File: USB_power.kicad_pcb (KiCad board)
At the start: 2 copper layers, 42.5 x 65.5 mm, 30 parts, among them J1 PWR_IN, J2 USB_A_Stacked, J3 Power_check, J4 USB_C_Receptacle_USB2.0_16P, J5 USB_A

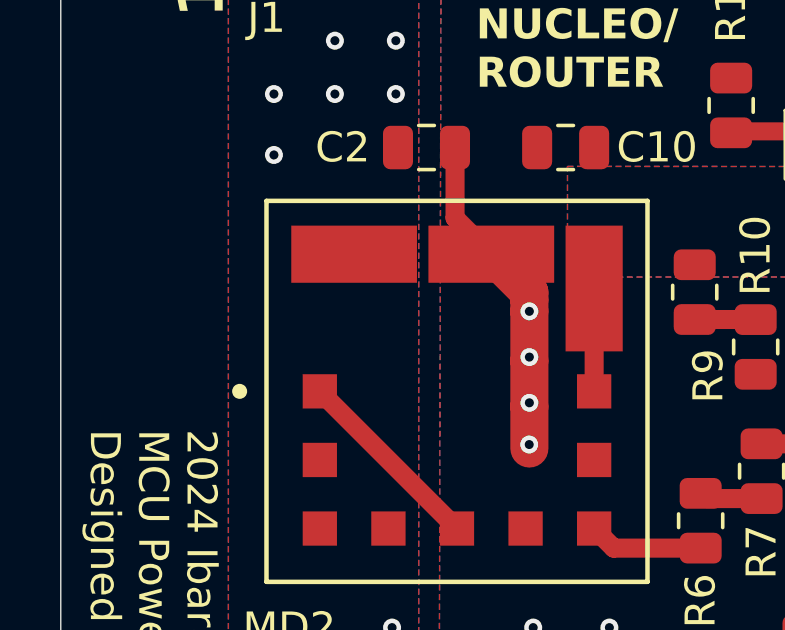
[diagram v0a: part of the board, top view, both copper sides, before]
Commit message: MD2直下BATTビア調整
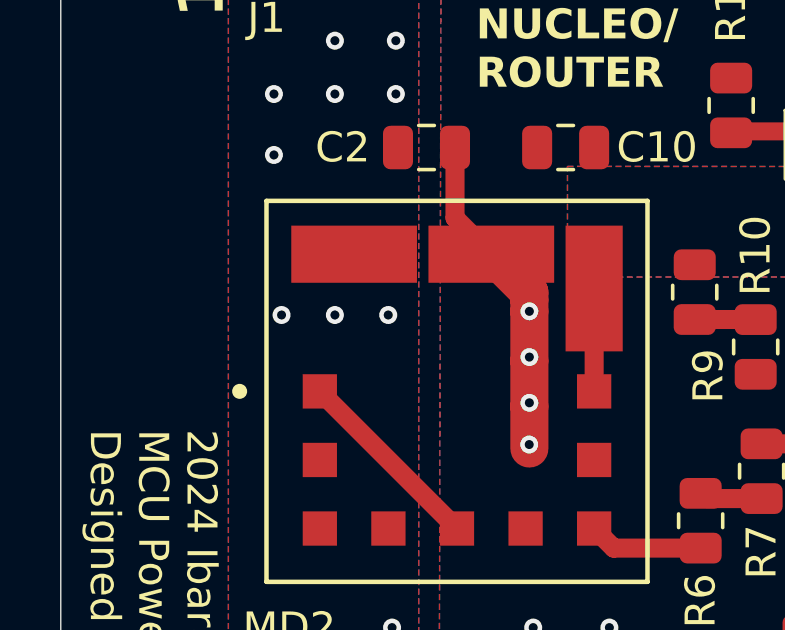
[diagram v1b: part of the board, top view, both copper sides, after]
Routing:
- net +BATT: vias 12 -> 15
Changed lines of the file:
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@@
+	)
+	(via
+		(at 136.906 98.552)
+		(size 0.6)
+		(drill 0.3)
+		(layers "F.Cu" "B.Cu")
+		(free yes)
+		(net 11)
+	)
+	(via
+		(at 135.128 98.552)
+		(size 0.6)
+		(drill 0.3)
+		(layers "F.Cu" "B.Cu")
+		(free yes)
+		(net 11)
 	)
 	(via
@@
 		(size 0.6)
 		(drill 0.3)
+		(layers "F.Cu" "B.Cu")
+		(free yes)
+		(net 11)
+	)
+	(via
+		(at 138.684 98.552)
+		(size 0.6)
+		(drill 0.3)

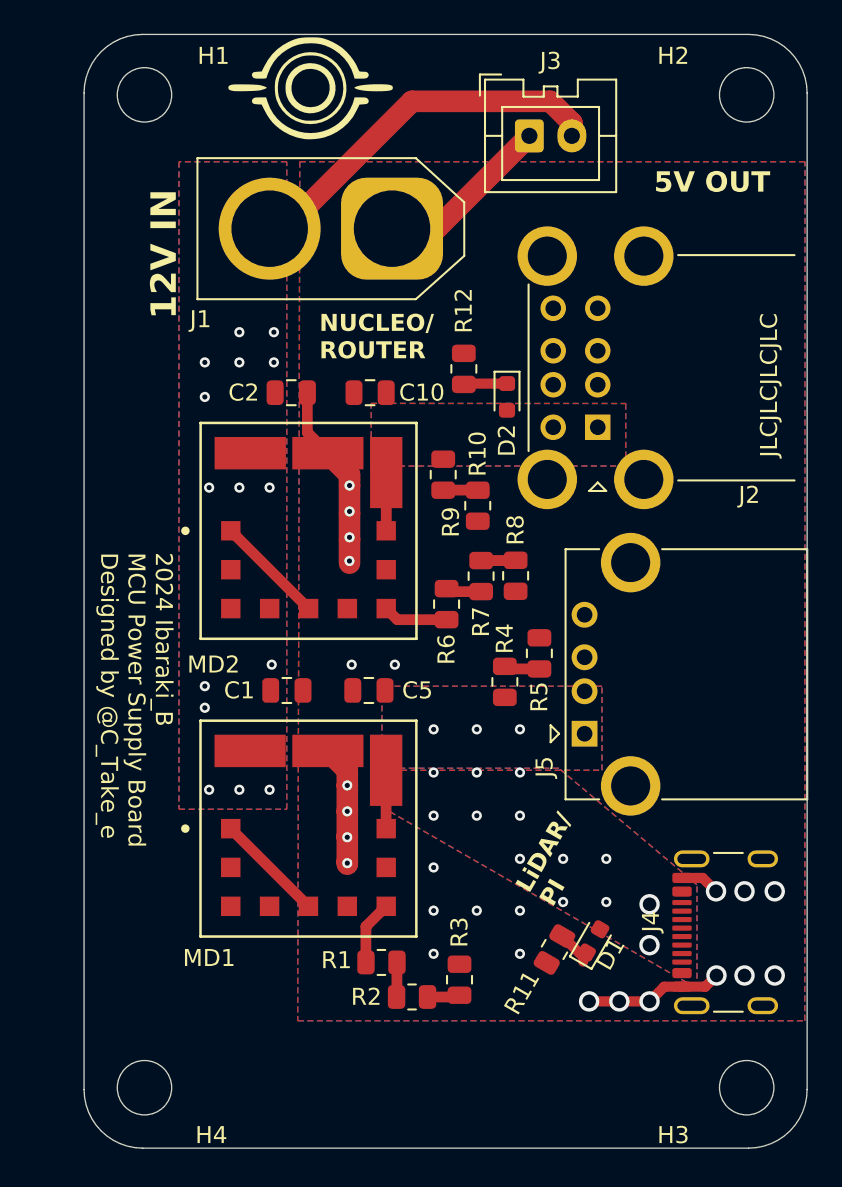
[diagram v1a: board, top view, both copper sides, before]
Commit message: Cのスペース詰めてGNDベタ回り込み
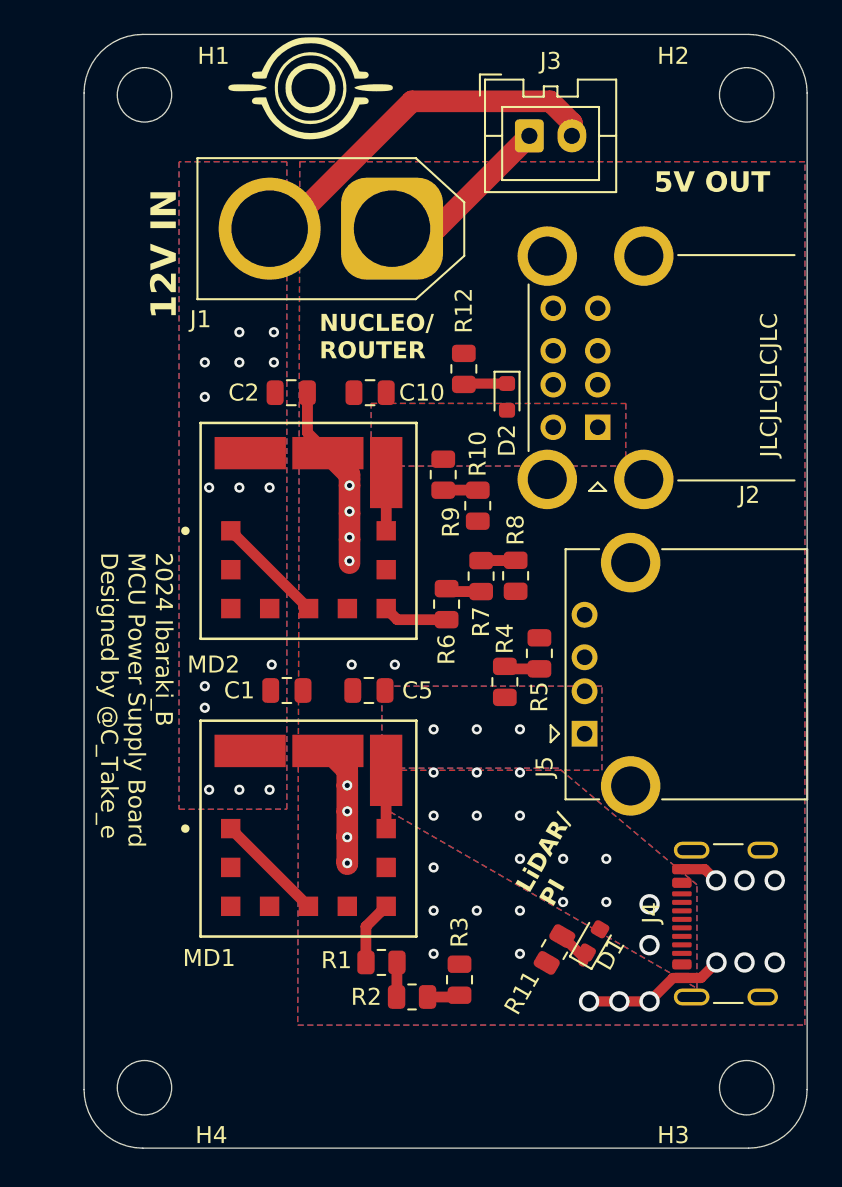
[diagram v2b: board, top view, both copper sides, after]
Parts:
- moved J4 0.51 mm to (166.6, 124.2)
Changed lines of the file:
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@@
 	(footprint "Connector_USB:USB_C_Receptacle_GCT_USB4105-xx-A_16P_TopMnt_Horizontal"
 		(layer "F.Cu")
-		(at 166.629518 124.719518 90)
+		(at 166.624 124.206 90)
 		(descr "USB 2.0 Type C Receptacle, GCT, 16P, top mounted, horizontal, 5A: https://gct.co/files/drawings/usb4105.pdf")
 		(tags "USB C Type-C Receptacle SMD USB 2.0 16P 16C USB4105-15-A USB4105-15-A-060 USB4105-15-A-120 USB4105-GF-A USB4105-GF-A-060 USB4105-GF-A-120")
@@
 	)
 	(segment
-		(start 164.318518 127.919518)
-		(end 162.949518 127.919518)
-		(width 0.6)
-		(layer "F.Cu")
-		(net 1)
-	)
-	(segment
 		(start 153.167518 104.653518)
 		(end 152.937018 104.653518)
@@
 	)
 	(segment
-		(start 164.166118 121.519518)
-		(end 162.949518 121.519518)
+		(start 162.944 121.006)
+		(end 164.293118 121.006)
 		(width 0.6)
 		(layer "F.Cu")
@@
 	)
 	(segment
-		(start 164.953118 122.306518)
-		(end 164.851118 122.408518)
+		(start 162.944 127.406)
+		(end 162.419036 127.406)
 		(width 0.6)
 		(layer "F.Cu")
@@
 	)
 	(segment
-		(start 162.949518 127.919518)
-		(end 161.905518 127.919518)
-		(width 0.6)
-		(layer "F.Cu")
-		(net 1)
-	)
-	(segment
 		(start 143.256 120.523)
 		(end 143.256 119.126)
@@
 	)
 	(segment
-		(start 164.978518 127.259518)
-		(end 164.318518 127.919518)
-		(width 0.6)
-		(layer "F.Cu")
-		(net 1)
-	)
-	(segment
 		(start 140.97 123.19)
 		(end 140.97 122.9995)
@@
 	)
 	(segment
-		(start 164.953118 122.306518)
-		(end 164.166118 121.519518)
+		(start 162.419036 127.406)
+		(end 161.041518 128.783518)
 		(width 0.6)
 		(layer "F.Cu")
@@
 	)
 	(segment
+		(start 162.944 127.406)
+		(end 164.064518 127.406)
+		(width 0.6)
+		(layer "F.Cu")
+		(net 1)
+	)
+	(segment
 		(start 143.388518 97.795518)
 		(end 143.388518 98.049518)
@@
 	)
 	(segment
+		(start 164.064518 127.406)
+		(end 164.978518 126.492)
+		(width 0.6)
+		(layer "F.Cu")
+		(net 1)
+	)
+	(segment
 		(start 157.485518 128.783518)
 		(end 161.041518 128.783518)
@@
 	)
 	(segment
+		(start 164.293118 121.006)
+		(end 164.953118 121.666)
+		(width 0.6)
+		(layer "F.Cu")
+		(net 1)
+	)
+	(segment
 		(start 143.256 117.602)
 		(end 143.256 116.078)
@@
 		(net 1)
 	)
-	(segment
-		(start 161.905518 127.919518)
-		(end 161.041518 128.783518)
-		(width 0.6)
-		(layer "F.Cu")
-		(net 1)
-	)
 	(via
 		(at 143.383 102.87)
@@
 	)
 	(via
-		(at 166.629518 122.306518)
+		(at 166.629518 121.666)
 		(size 1.2)
 		(drill 0.8)
@@
 	)
 	(via
-		(at 164.978518 127.259518)
+		(at 164.978518 126.492)
 		(size 1.2)
 		(drill 0.8)
@@
 	)
 	(via
-		(at 164.953118 122.306518)
+		(at 164.953118 121.666)
 		(size 1.2)
 		(drill 0.8)
@@
 	)
 	(via
-		(at 166.629518 127.259518)
+		(at 166.629518 126.492)
 		(size 1.2)
 		(drill 0.8)
@@
 	)
 	(via
-		(at 168.407518 127.259518)
+		(at 168.407518 126.492)
 		(size 1.2)
 		(drill 0.8)
@@
 	)
 	(via
-		(at 168.407518 122.306518)
+		(at 168.407518 121.666)
 		(size 1.2)
 		(drill 0.8)
@@
 		(polygon
 			(pts
-				(xy 140.462 79.375) (xy 140.340518 129.926518) (xy 170.18 129.921) (xy 170.185518 79.375)
+				(xy 140.462 79.375) (xy 140.340518 130.180518) (xy 170.18 130.175) (xy 170.185518 79.375)
 			)
 		)

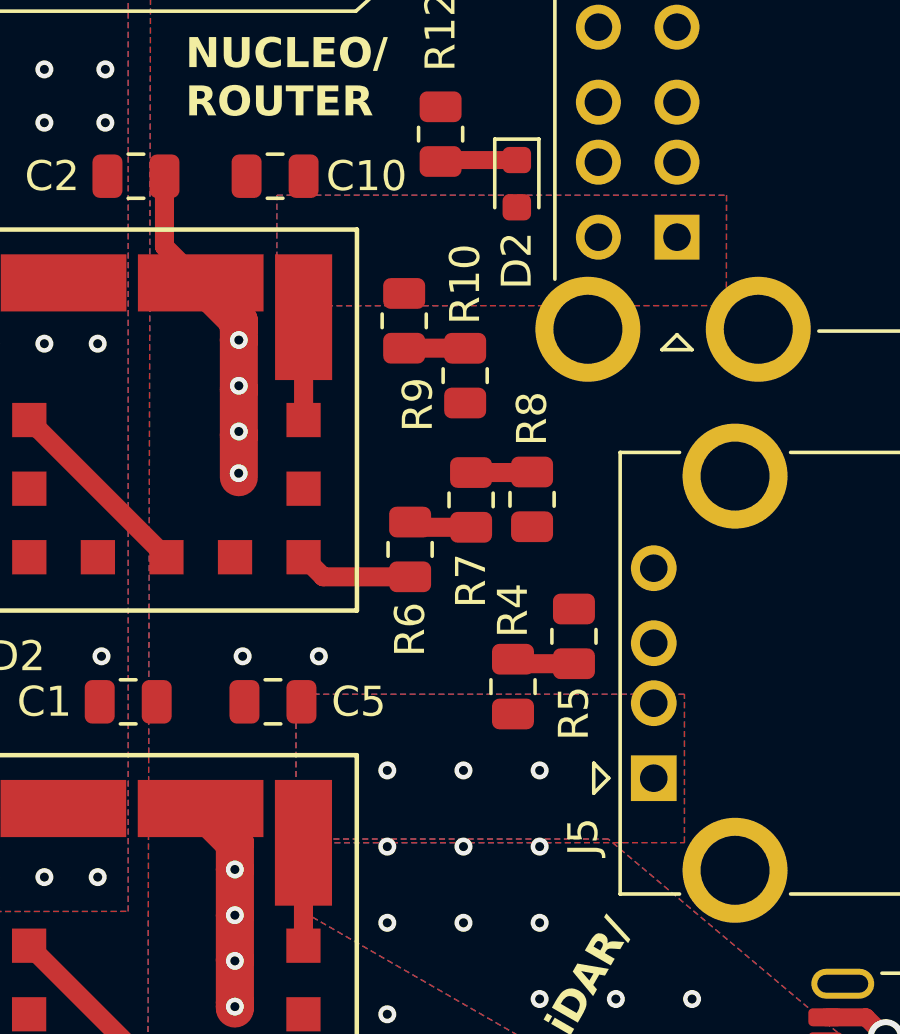
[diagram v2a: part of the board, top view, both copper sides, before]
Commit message: MD2周り抵抗ゴン詰め、MD1系統スタックコネクタ化計画
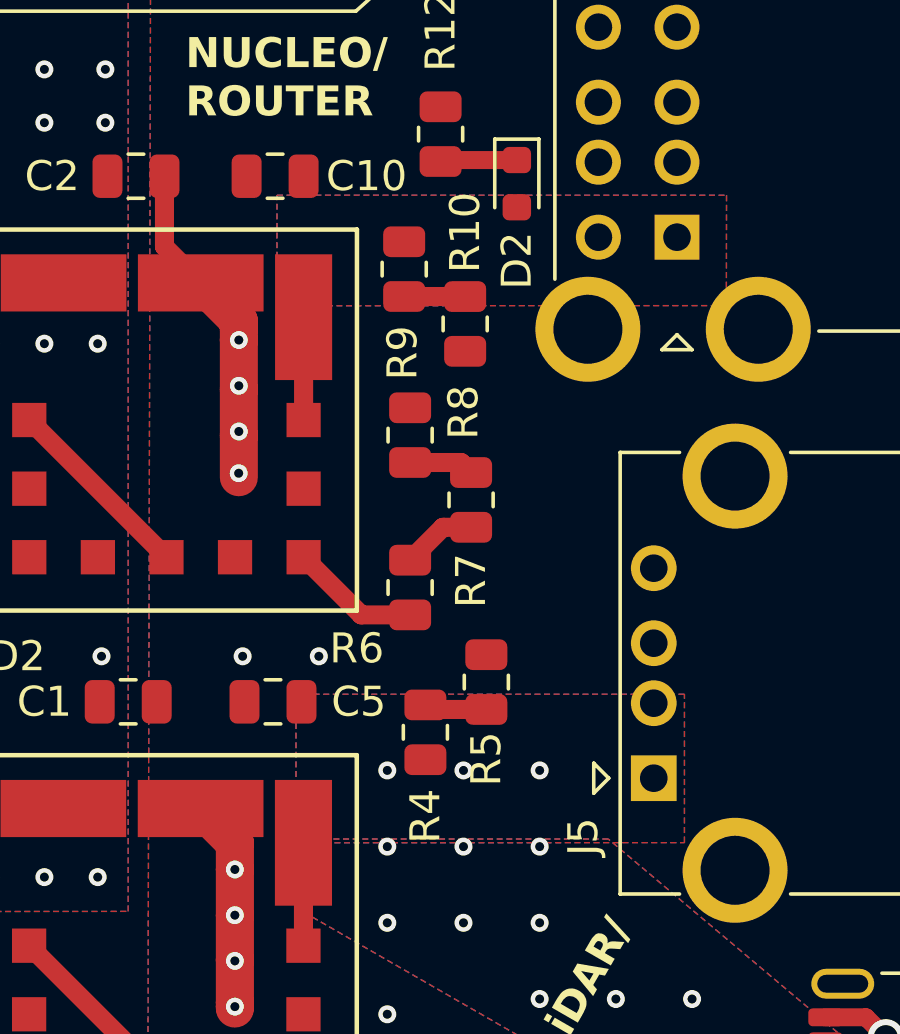
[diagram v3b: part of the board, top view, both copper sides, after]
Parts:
- moved R8 4.59 mm to (149.1, 101.6), turned to 90 degrees
- moved R4 3.29 mm to (149.6, 111.5)
- moved R5 3.29 mm to (151.6, 109.8)
- moved R9 1.72 mm to (148.9, 96.1)
- moved R10 1.72 mm to (150.9, 97.9)
- moved R6 1.27 mm to (149.1, 106.7)
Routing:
- net Net-(MD2-TRIM): track 3.82 -> 4.35 mm
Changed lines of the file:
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@@
 	(footprint "Resistor_SMD:R_0805_2012Metric"
 		(layer "F.Cu")
-		(at 148.900318 97.79 -90)
+		(at 148.900318 96.0666 -90)
 		(descr "Resistor SMD 0805 (2012 Metric), square (rectangular) end terminal, IPC_7351 nominal, (Body size source: IPC-SM-782 page 72, https://www.pcb-3d.com/wordpress/wp-content/uploads/ipc-sm-782a_amendment_1_and_2.pdf), generated with kicad-footprint-generator")
 		(tags "resistor")
 		(property "Reference" "R9"
-			(at 2.7921 -0.4572 90)
+			(at 2.7921 0.056318 90)
 			(layer "F.SilkS")
 			(effects
@@
 	(footprint "Resistor_SMD:R_0805_2012Metric"
 		(layer "F.Cu")
-		(at 150.932318 99.6169 -90)
+		(at 150.932318 97.8935 -90)
 		(descr "Resistor SMD 0805 (2012 Metric), square (rectangular) end terminal, IPC_7351 nominal, (Body size source: IPC-SM-782 page 72, https://www.pcb-3d.com/wordpress/wp-content/uploads/ipc-sm-782a_amendment_1_and_2.pdf), generated with kicad-footprint-generator")
 		(tags "resistor")
@@
 	(footprint "Resistor_SMD:R_0805_2012Metric"
 		(layer "F.Cu")
-		(at 152.527 109.982 90)
+		(at 149.606 111.506 90)
 		(descr "Resistor SMD 0805 (2012 Metric), square (rectangular) end terminal, IPC_7351 nominal, (Body size source: IPC-SM-782 page 72, https://www.pcb-3d.com/wordpress/wp-content/uploads/ipc-sm-782a_amendment_1_and_2.pdf), generated with kicad-footprint-generator")
 		(tags "resistor")
 		(property "Reference" "R4"
-			(at 2.5381 0 90)
+			(at -2.794 0 90)
 			(layer "F.SilkS")
 			(effects
@@
 	(footprint "Resistor_SMD:R_0805_2012Metric"
 		(layer "F.Cu")
-		(at 154.559 108.3075 90)
+		(at 151.638 109.8315 90)
 		(descr "Resistor SMD 0805 (2012 Metric), square (rectangular) end terminal, IPC_7351 nominal, (Body size source: IPC-SM-782 page 72, https://www.pcb-3d.com/wordpress/wp-content/uploads/ipc-sm-782a_amendment_1_and_2.pdf), generated with kicad-footprint-generator")
 		(tags "resistor")
@@
 	(footprint "Resistor_SMD:R_0805_2012Metric"
 		(layer "F.Cu")
-		(at 149.098 105.41 90)
+		(at 149.098 106.68 90)
 		(descr "Resistor SMD 0805 (2012 Metric), square (rectangular) end terminal, IPC_7351 nominal, (Body size source: IPC-SM-782 page 72, https://www.pcb-3d.com/wordpress/wp-content/uploads/ipc-sm-782a_amendment_1_and_2.pdf), generated with kicad-footprint-generator")
 		(tags "resistor")
 		(property "Reference" "R6"
-			(at -2.667 0 -90)
+			(at -2.032 -1.778 0)
 			(layer "F.SilkS")
 			(effects
@@
 	(footprint "Resistor_SMD:R_0805_2012Metric"
 		(layer "F.Cu")
-		(at 153.162 103.741018 -90)
+		(at 149.098 101.6 90)
 		(descr "Resistor SMD 0805 (2012 Metric), square (rectangular) end terminal, IPC_7351 nominal, (Body size source: IPC-SM-782 page 72, https://www.pcb-3d.com/wordpress/wp-content/uploads/ipc-sm-782a_amendment_1_and_2.pdf), generated with kicad-footprint-generator")
 		(tags "resistor")
 		(property "Reference" "R8"
-			(at -2.6905 0 90)
+			(at 0.762 1.778 90)
 			(layer "F.SilkS")
 			(effects
@@
 		)
 		(property "Footprint" "Resistor_SMD:R_0805_2012Metric"
-			(at 0 0 -90)
+			(at 0 0 90)
 			(unlocked yes)
 			(layer "F.Fab")
@@
 		)
 		(property "Datasheet" ""
-			(at 0 0 -90)
+			(at 0 0 90)
 			(unlocked yes)
 			(layer "F.Fab")
@@
 		)
 		(property "Description" "Resistor"
-			(at 0 0 -90)
+			(at 0 0 90)
 			(unlocked yes)
 			(layer "F.Fab")
@@
 		(attr smd)
 		(fp_line
-			(start -0.227064 0.735)
-			(end 0.227064 0.735)
+			(start -0.227064 -0.735)
+			(end 0.227064 -0.735)
 			(stroke
 				(width 0.12)
@@
 		)
 		(fp_line
-			(start -0.227064 -0.735)
-			(end 0.227064 -0.735)
+			(start -0.227064 0.735)
+			(end 0.227064 0.735)
 			(stroke
 				(width 0.12)
@@
 		)
 		(fp_line
-			(start -1.68 0.95)
-			(end -1.68 -0.95)
+			(start 1.68 -0.95)
+			(end 1.68 0.95)
 			(stroke
 				(width 0.05)
@@
 		)
 		(fp_line
-			(start 1.68 0.95)
-			(end -1.68 0.95)
+			(start -1.68 -0.95)
+			(end 1.68 -0.95)
 			(stroke
 				(width 0.05)
@@
 		)
 		(fp_line
-			(start -1.68 -0.95)
-			(end 1.68 -0.95)
+			(start 1.68 0.95)
+			(end -1.68 0.95)
 			(stroke
 				(width 0.05)
@@
 		)
 		(fp_line
-			(start 1.68 -0.95)
-			(end 1.68 0.95)
+			(start -1.68 0.95)
+			(end -1.68 -0.95)
 			(stroke
 				(width 0.05)
@@
 		)
 		(fp_line
-			(start -1 0.625)
-			(end -1 -0.625)
+			(start 1 -0.625)
+			(end 1 0.625)
 			(stroke
 				(width 0.1)
@@
 		)
 		(fp_line
-			(start 1 0.625)
-			(end -1 0.625)
+			(start -1 -0.625)
+			(end 1 -0.625)
 			(stroke
 				(width 0.1)
@@
 		)
 		(fp_line
-			(start -1 -0.625)
-			(end 1 -0.625)
+			(start 1 0.625)
+			(end -1 0.625)
 			(stroke
 				(width 0.1)
@@
 		)
 		(fp_line
-			(start 1 -0.625)
-			(end 1 0.625)
+			(start -1 0.625)
+			(end -1 -0.625)
 			(stroke
 				(width 0.1)
@@
 		)
 		(pad "1" smd roundrect
-			(at -0.9125 0 270)
+			(at -0.9125 0 90)
 			(size 1.025 1.4)
 			(layers "F.Cu" "F.Paste" "F.Mask")
@@
 		)
 		(pad "2" smd roundrect
-			(at 0.9125 0 270)
+			(at 0.9125 0 90)
 			(size 1.025 1.4)
 			(layers "F.Cu" "F.Paste" "F.Mask")
@@
 	)
 	(segment
-		(start 153.167518 104.653518)
-		(end 152.937018 104.653518)
-		(width 0.635)
-		(layer "F.Cu")
-		(net 1)
-	)
-	(segment
 		(start 143.256 116.078)
 		(end 143.256 115.189)
@@
 	)
 	(segment
-		(start 152.6775 109.22)
-		(end 152.527 109.0695)
+		(start 149.7565 110.744)
+		(end 149.606 110.5935)
 		(width 0.635)
 		(layer "F.Cu")
@@
 	)
 	(segment
-		(start 154.559 109.22)
-		(end 152.6775 109.22)
+		(start 151.638 110.744)
+		(end 149.7565 110.744)
 		(width 0.635)
 		(layer "F.Cu")
@@
 	)
 	(segment
-		(start 146.2005 106.3225)
-		(end 149.098 106.3225)
+		(start 147.4705 107.5925)
+		(end 149.098 107.5925)
 		(width 0.635)
 		(layer "F.Cu")
@@
 	(segment
 		(start 145.547518 105.669518)
-		(end 146.2005 106.3225)
+		(end 147.4705 107.5925)
 		(width 0.635)
 		(layer "F.Cu")
@@
 	)
 	(segment
-		(start 149.272 104.6715)
-		(end 149.098 104.4975)
+		(start 151.13 104.6715)
+		(end 150.194 104.6715)
 		(width 0.635)
 		(layer "F.Cu")
@@
 	)
 	(segment
-		(start 151.13 104.6715)
-		(end 149.272 104.6715)
+		(start 150.194 104.6715)
+		(end 149.098 105.7675)
 		(width 0.635)
 		(layer "F.Cu")
@@
 	)
 	(segment
-		(start 153.144018 102.8465)
-		(end 153.162 102.828518)
+		(start 150.796 102.5125)
+		(end 151.13 102.8465)
 		(width 0.635)
 		(layer "F.Cu")
@@
 	)
 	(segment
-		(start 151.13 102.8465)
-		(end 153.144018 102.8465)
+		(start 149.098 102.5125)
+		(end 150.796 102.5125)
 		(width 0.635)
 		(layer "F.Cu")
@@
 	)
 	(segment
-		(start 148.900318 98.7025)
-		(end 150.930418 98.7025)
+		(start 148.900318 96.9791)
+		(end 150.930418 96.9791)
 		(width 0.635)
 		(layer "F.Cu")
@@
 	)
 	(segment
-		(start 150.930418 98.7025)
-		(end 150.932318 98.7044)
+		(start 150.930418 96.9791)
+		(end 150.932318 96.981)
 		(width 0.635)
 		(layer "F.Cu")
